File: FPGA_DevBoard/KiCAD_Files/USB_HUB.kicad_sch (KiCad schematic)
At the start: 35 parts, among them J5 USB-A1HSW6, J6 USB-A1HSW6, U10 NCP380HSN05AAT1G, U17 CP2102-GMR, U7 USBLC6-2SC6, U8 USBLC6-2SC6, U9 NCP380HSN05AAT1G, X1 24MHz

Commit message: Updated ESD for both the USB hub outputs and GPIO output
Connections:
- net USB1_N: now also U7.1 (IO_1); no longer U7.4 (IO_2)
- net USB1_P: now also U7.4 (IO_2); no longer U7.1 (IO_1)
- net USB2_N: now also U8.3 (IO_2); no longer U8.6 (IO_1)
- net USB2_P: now also U8.6 (IO_1); no longer U8.3 (IO_2)

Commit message: forgot to save schematic when pushing last commit
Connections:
- net USB1_N: now also U7.3 (IO_2), U7.4 (IO_2); no longer U7.1 (IO_1), U7.6 (IO_1)
- net USB1_P: now also U7.1 (IO_1), U7.6 (IO_1); no longer U7.3 (IO_2), U7.4 (IO_2)

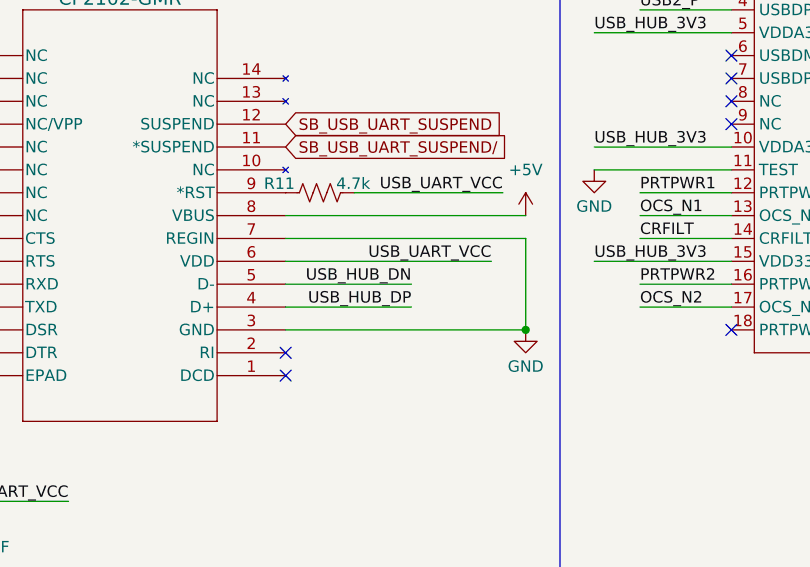
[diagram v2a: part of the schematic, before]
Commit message: Updated the NBSB IO to not go to input only, need to change this on the layout. Updated the FPGA clk to go to a positive differential signal with MCRR - need to change on layout. Updated the USB-UART bridge to not have Regin grounded - need to change on layout.
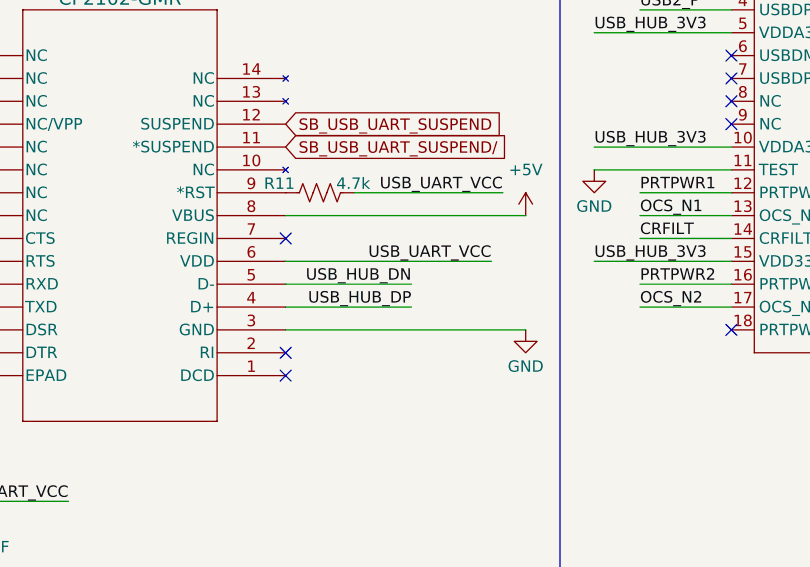
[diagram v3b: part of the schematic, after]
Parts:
- U11: value ~ -> (none)
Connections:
- net GND: no longer U17.7 (REGIN)
- no-connect marks 13 -> 14

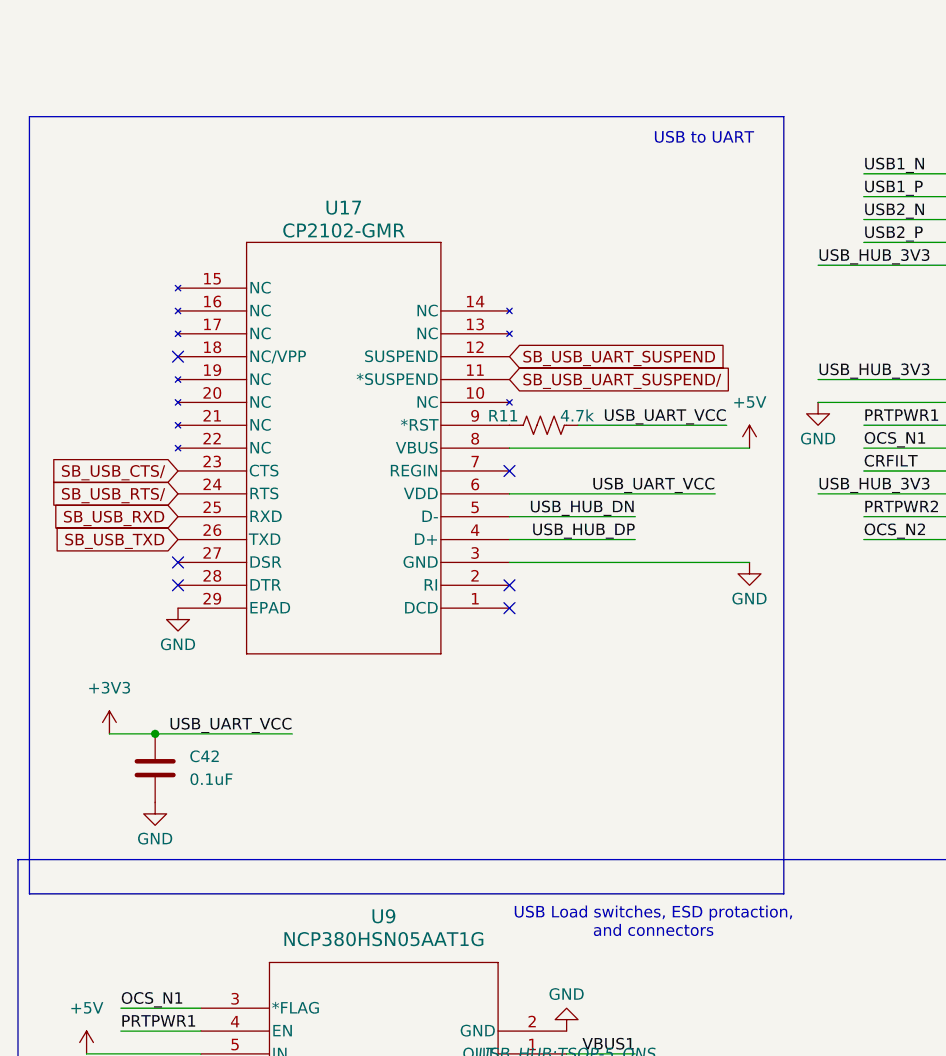
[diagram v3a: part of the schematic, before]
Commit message: OK I PULL UP
Added pull up resistors to SPI CS, pull down to GPIO12, redid vga bus lines. This also might include the FPGA clock being correct? Idk if that was committed before
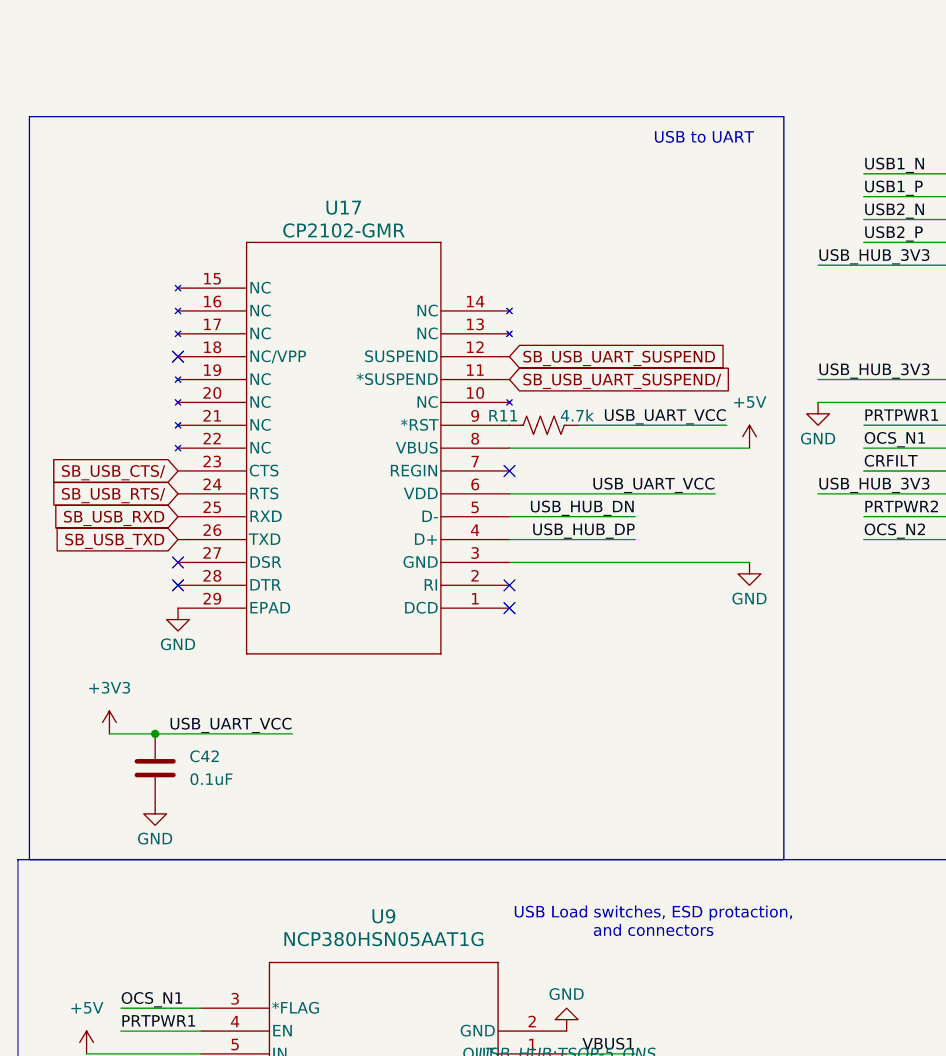
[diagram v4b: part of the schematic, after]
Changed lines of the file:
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@@
 	(rectangle
 		(start 13.97 24.13)
-		(end 97.79 110.49)
+		(end 97.79 106.68)
 		(stroke
 			(width 0)

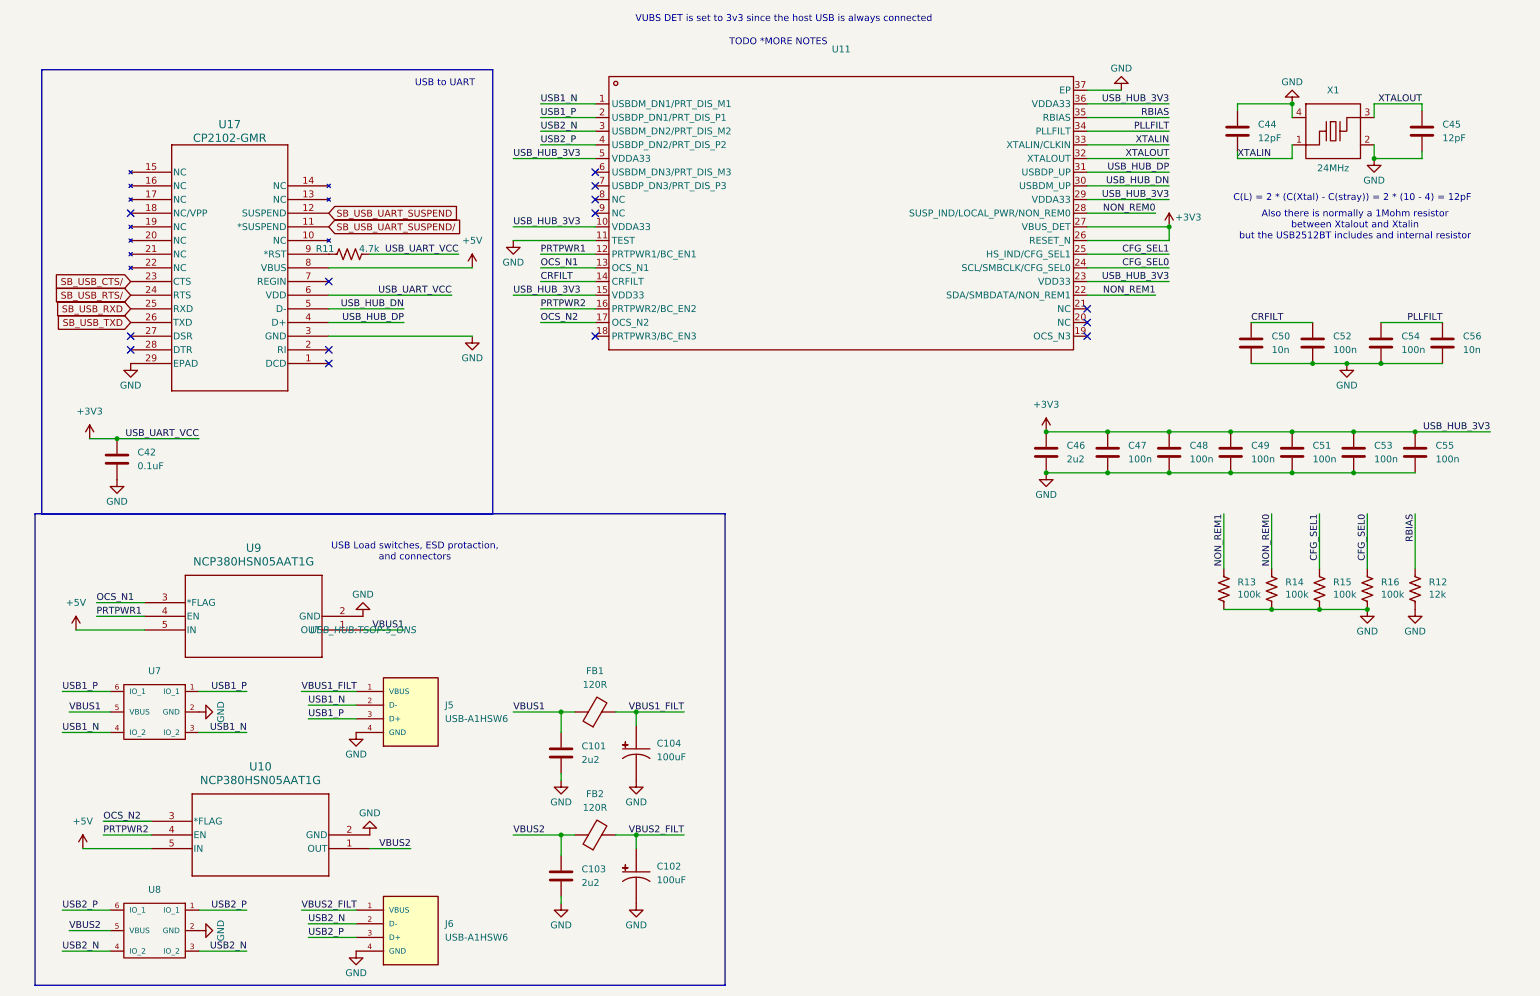
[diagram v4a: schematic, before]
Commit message: Universal Serial Bussin it down
Replaced the USB Hub with the new USB Hosts, added a clock reset button, moved some things on the silk screen.
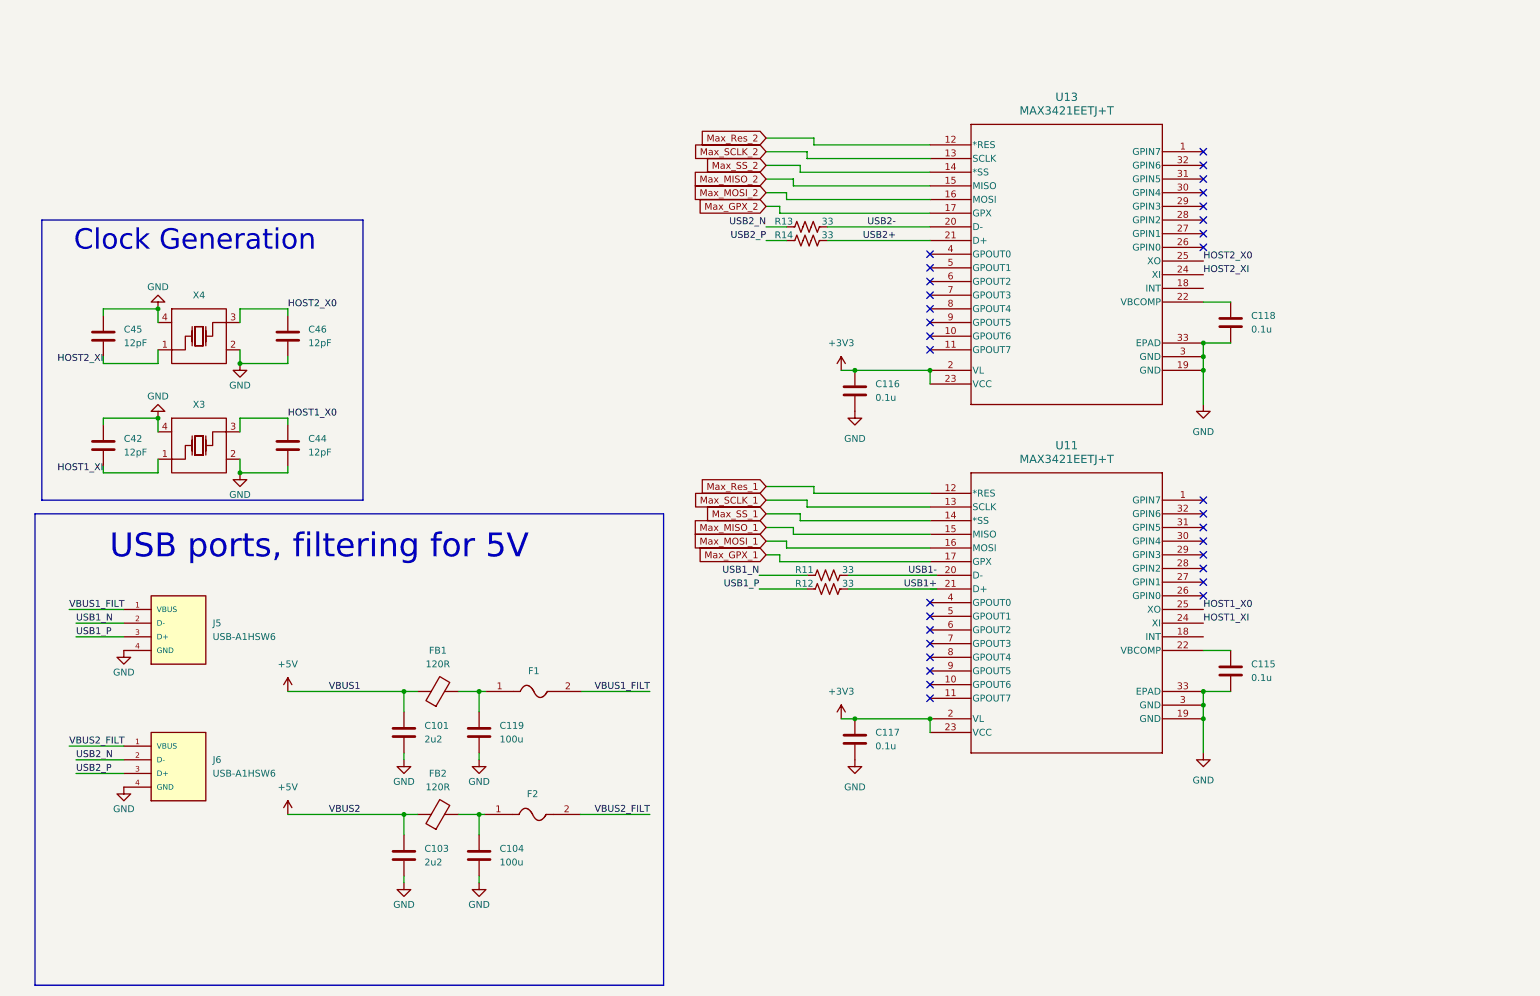
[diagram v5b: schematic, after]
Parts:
- removed C102, C104: 100uF, USB_HUB:CAP-SMD_BD6.3-L6.6-W6.6-FD, symbol USB_HUB:RVT0J101M0605
- removed C47, C48, C49, C51, C52, C53, C54, C55: 100n, Capacitor_SMD:C_0402_1005Metric, symbol Device:C
- removed C50, C56: 10n, Capacitor_SMD:C_0402_1005Metric, symbol Device:C
- removed R15, R16: 100k, Resistor_SMD:R_0402_1005Metric, symbol Device:R_US
- removed U10, U9: NCP380HSN05AAT1G, USB_HUB:TSOP-5_ONS, symbol Test:NCP380HSN05AAT1G
- removed U11: (no value), USB_HUB:USB2513BM2, symbol USB_HUB:USB2513B/M2
- removed U17: CP2102-GMR, USB_HUB:CP2102_GMR_SIL, symbol USB_HUB:CP2102-GMR
- removed U7, U8: USBLC6-2SC6, USB_HUB:SOT95P280X145-6N, symbol Test:USBLC6-2SC6
- removed X1: 24MHz, USB_HUB:CRYSTAL-SMD_4P-L2.0-W1.6-BL, symbol USB_HUB:XL7EL89CMI-111YLC-24M
- added C104, C119: 100u, Capacitor_SMD:C_0805_2012Metric, symbol Device:C
- added C115, C116, C117, C118: 0.1u, Capacitor_SMD:C_0402_1005Metric, symbol Device:C
- added F1, F2: (no value), USB_HUB:F1812, symbol USB_HUB:SMD1812P050TF
- added U11, U13: MAX3421EETJ+T, USB_HUB:MAX3421EETJ_T, symbol USB_HUB:MAX3421EETJ+T
- added X3, X4: 12MHz, FPGA&MCU:CRYSTAL-SMD_4P-L3.2-W2.5-BL, symbol FPGA&MCU:X322512MMB4SI
- C101, C103: footprint Capacitor_SMD:C_0201_0603Metric -> Capacitor_SMD:C_0402_1005Metric
- C42: value 0.1uF -> 12pF
- C46: value 2u2 -> 12pF; footprint Capacitor_SMD:C_0201_0603Metric -> Capacitor_SMD:C_0402_1005Metric
- R11: value 4.7k -> 33; footprint Resistor_SMD:R_0201_0603Metric -> Resistor_SMD:R_0402_1005Metric
- R12: value 12k -> 33
- R13, R14: value 100k -> 33
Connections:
- net NON_REM0 is gone; now on net USB2_P: R14.1
- net NON_REM1 is gone; now on net USB2_N: R13.1
- net RBIAS is gone; now on net USB1_P: R12.1
- net VBUS1 is gone; now on net +5V: C101.1, FB1.1
- net VBUS2 is gone; now on net +5V: C103.1, FB2.1
- net XTALIN is gone; now on net GND: C44.2
- net XTALOUT is gone; now on net GND: C45.1
- net +3V3: now also C116.1, C117.1, U11.2 (VL), U11.23 (VCC), U13.2 (VL), U13.23 (VCC); no longer C42.1, C46.1, R11.2
- net GND: now also C42.1, C104.2, C115.2, C116.2, C117.2, C118.2, C119.2, U11.19 (GND), U11.3 (GND), U11.33 (EPAD), U13.19 (GND), U13.3 (GND), U13.33 (EPAD), X3.2 (GND), X3.4 (GND), X4.2 (GND), X4.4 (GND); no longer C42.2, C44.1, C45.2, R12.2, R13.2, R14.2
- net USB1_N: now also R11.1
- net VBUS1_FILT: now also F1.2; no longer FB1.2
- net VBUS2_FILT: now also F2.2; no longer FB2.2
- new net: C118.1, U13.22 (VBCOMP)
- new net: C104.1, F2.1, FB2.2
- new net: C119.1, F1.1, FB1.2
- new net: C115.1, U11.22 (VBCOMP)
- new net HOST1_X0: C44.1, U11.25 (XO), X3.3 (OSC2)
- new net HOST1_XI: C42.2, U11.24 (XI), X3.1 (OSC1)
- new net HOST2_X0: C46.1, U13.25 (XO), X4.3 (OSC2)
- new net HOST2_XI: C45.2, U13.24 (XI), X4.1 (OSC1)
- new net Max_GPX_1: U11.17 (GPX)
- new net Max_GPX_2: U13.17 (GPX)
- new net Max_MISO_1: U11.15 (MISO)
- new net Max_MISO_2: U13.15 (MISO)
- new net Max_MOSI_1: U11.16 (MOSI)
- new net Max_MOSI_2: U13.16 (MOSI)
- new net Max_Res_1: U11.12 (*RES)
- new net Max_Res_2: U13.12 (*RES)
- new net Max_SCLK_1: U11.13 (SCLK)
- new net Max_SCLK_2: U13.13 (SCLK)
- new net Max_SS_1: U11.14 (*SS)
- new net Max_SS_2: U13.14 (*SS)
- new net USB1+: R12.2
- new net USB1-: R11.2
- new net USB2+: R14.2, U13.21 (D+)
- new net USB2-: R13.2, U13.20 (D-)
- no-connect marks 14 -> 32
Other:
- note added: "Clock Generation"
- note added: "USB ports, filtering for 5V"
- note removed: "Also there is normally a 1Mohm resistor between Xtalout and Xtalin but the USB2512BT includes and internal resistor"
- note removed: "C(L) = 2 * (C(Xtal) - C(stray)) = 2 * (10 - 4) = 12pF"
- note removed: "TODO *MORE NOTES"
- note removed: "USB Load switches, ESD protaction, and connectors"
- note removed: "USB to UART"
- note removed: "VUBS DET is set to 3v3 since the host USB is always connected"
- moved on the sheet: C101, C103, FB1, FB2, J5, J6

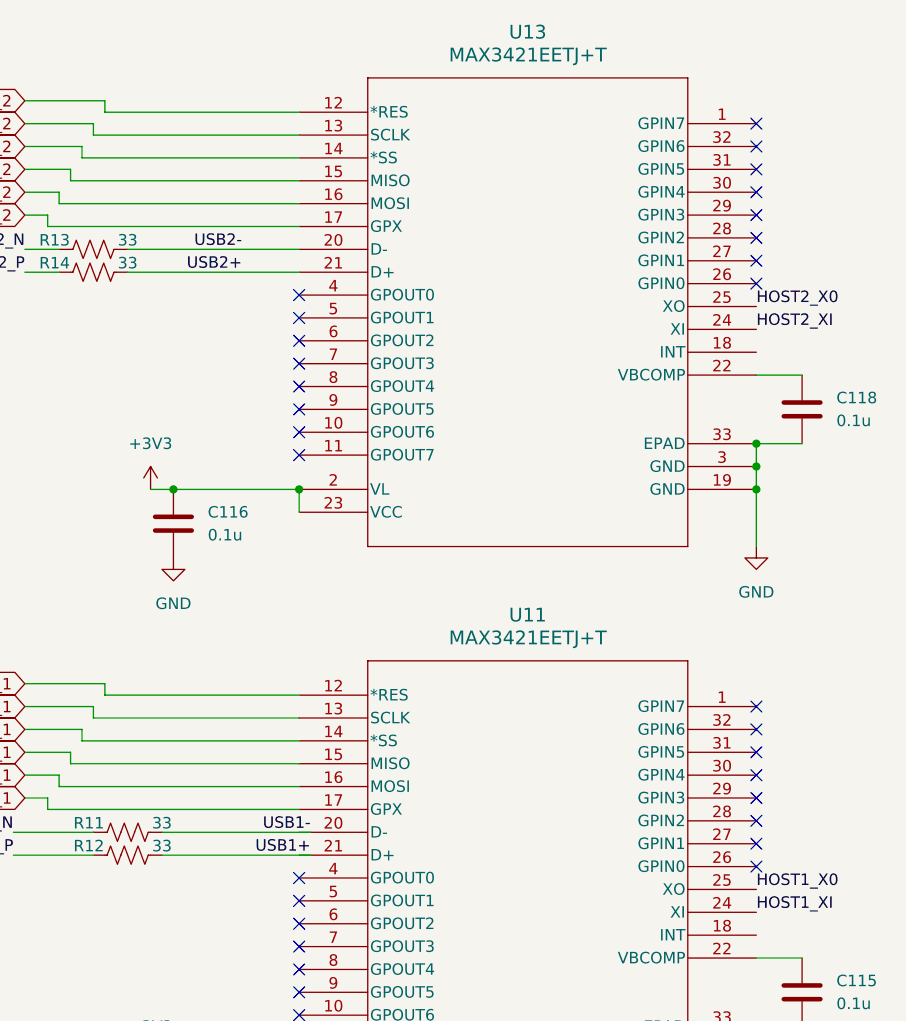
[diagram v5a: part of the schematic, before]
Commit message: VGA LENGTH MATCH, LED
Length matched the VGA, updated the GPIO to use the usb host gpio, added some leds and fixed the silkscreen more
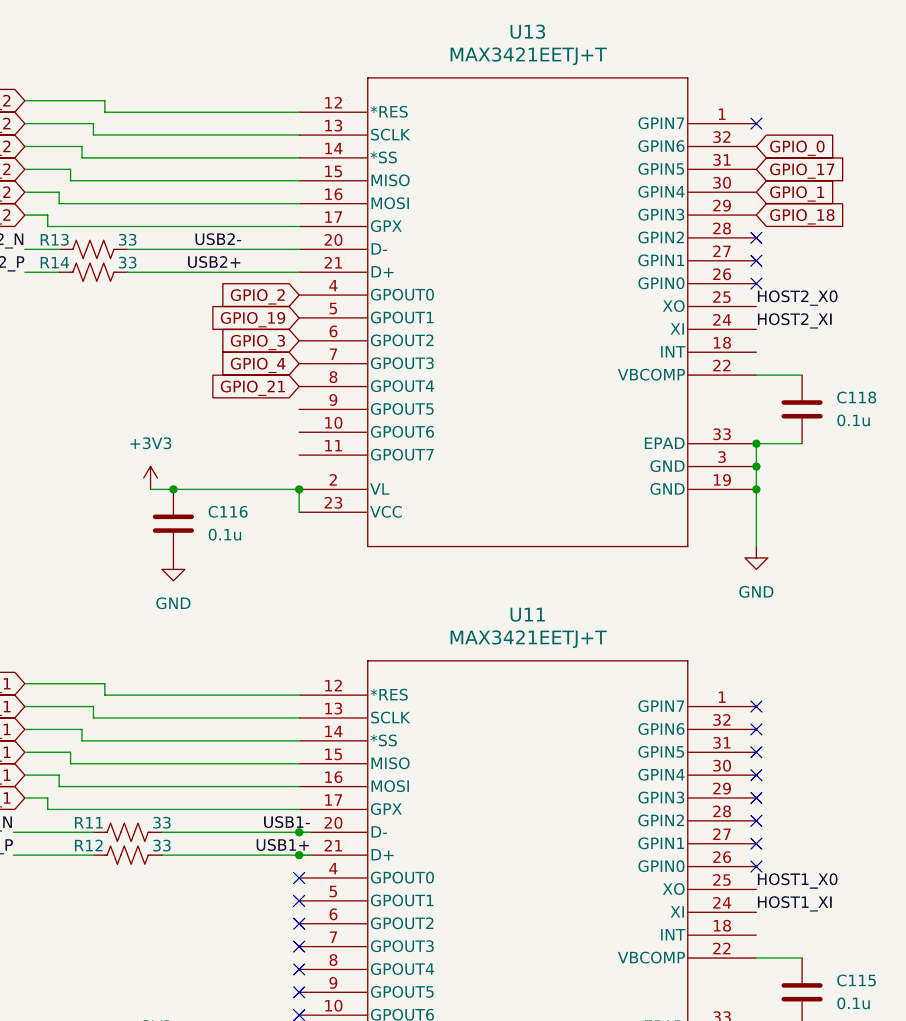
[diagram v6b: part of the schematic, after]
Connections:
- net USB1+: now also U11.21 (D+)
- net USB1-: now also U11.20 (D-)
- net GPIO_18: now reaches U13.29 (GPIN3)
- net GPIO_1: now reaches U13.30 (GPIN4)
- net GPIO_17: now reaches U13.31 (GPIN5)
- net GPIO_0: now reaches U13.32 (GPIN6)
- net GPIO_2: now reaches U13.4 (GPOUT0)
- net GPIO_19: now reaches U13.5 (GPOUT1)
- net GPIO_3: now reaches U13.6 (GPOUT2)
- net GPIO_4: now reaches U13.7 (GPOUT3)
- net GPIO_21: now reaches U13.8 (GPOUT4)
- no-connect marks 32 -> 20
